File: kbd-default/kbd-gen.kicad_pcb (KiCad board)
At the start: 2 copper layers, 284.6 x 94.2 mm, 142 parts, among them CN1 BTB, CN2 BTB

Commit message: update kbd-default
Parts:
- removed the ? at (309.1, 81.9)
- removed the ? at (310.3, 81.9)
- removed the ? at (87.8, 82.5)
- added ?: , , F.Cu at (91.6, 83.0)
- added ?: , , F.Cu at (308.7, 83.0)
- added ?: , , F.Cu at (61.4, 159.2)
- added ?: , , F.Cu at (301.8, 82.8)
- added ?: , , F.Cu at (346.4, 158.4)
- added ?: , , F.Cu at (347.0, 65.0)
- added ?: , , F.Cu at (62.9, 65.2)
- moved ? 0.62 mm to (170.5, 68.1)
- moved ? 0.46 mm to (86.5, 83.0)
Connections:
- CN1 pad 33: (no net) -> VCC
- CN1 pad 34: (no net) -> GND
- CN2 pad 33: (no net) -> VCC
- CN2 pad 34: (no net) -> GND
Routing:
- net VCC: track 1589.7 -> 1602.3 mm, vias 16 -> 17
- net r4: track 391.7 -> 383.9 mm, vias 4 -> 2
- net c1: track 163.5 -> 167.5 mm
- net c3: track 139.0 -> 141.8 mm
- net r2: track 322.5 -> 319.8 mm
- net led2_17: track 148.7 -> 150.9 mm, vias 5 -> 6
- net r5: track 491.5 -> 489.6 mm
- net GND: track 1577.0 -> 1578.8 mm, vias 15 -> 14
- net S312_314: track 41.2 -> 42.9 mm
- net r3: track 408.2 -> 409.9 mm
- net S48_58: track 28.8 -> 27.3 mm
- net c4: track 83.3 -> 84.7 mm
- net r1: track 286.8 -> 288.2 mm
- net S37_38: track 29.5 -> 30.7 mm
- net S113_114: track 41.0 -> 39.9 mm
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
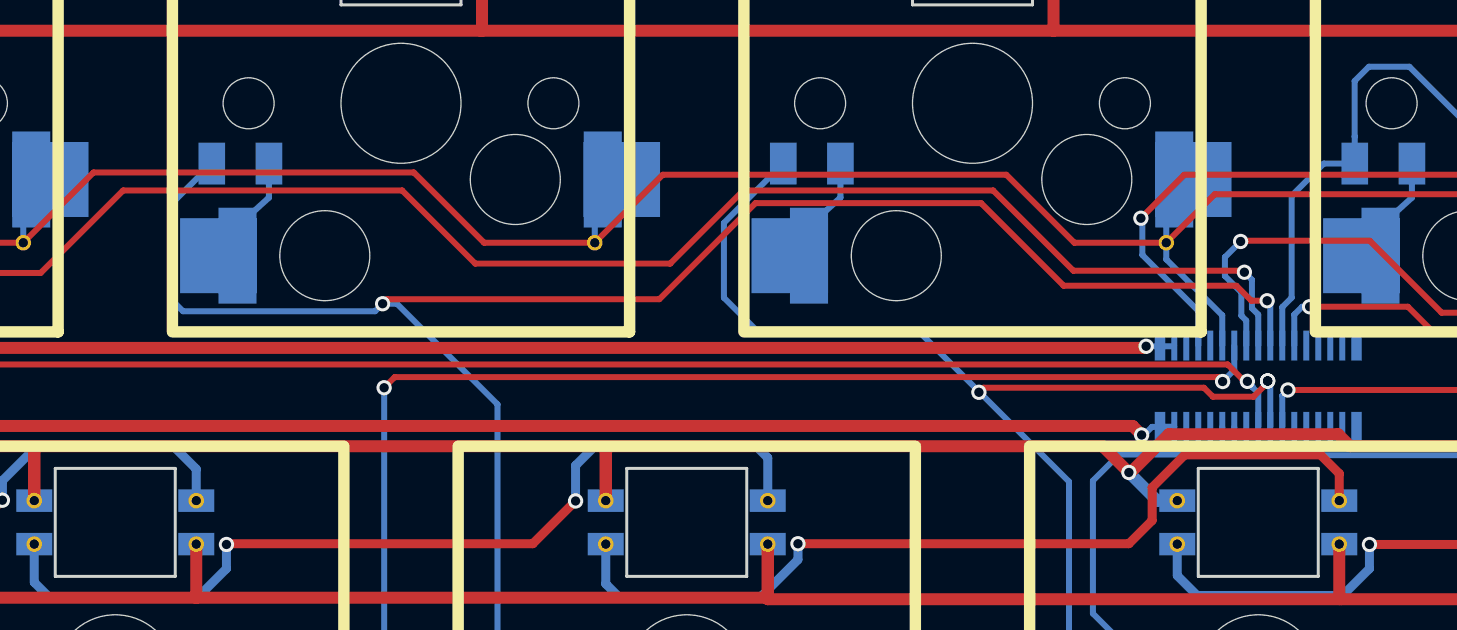
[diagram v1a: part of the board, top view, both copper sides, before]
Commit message: update default(boa) v0.2
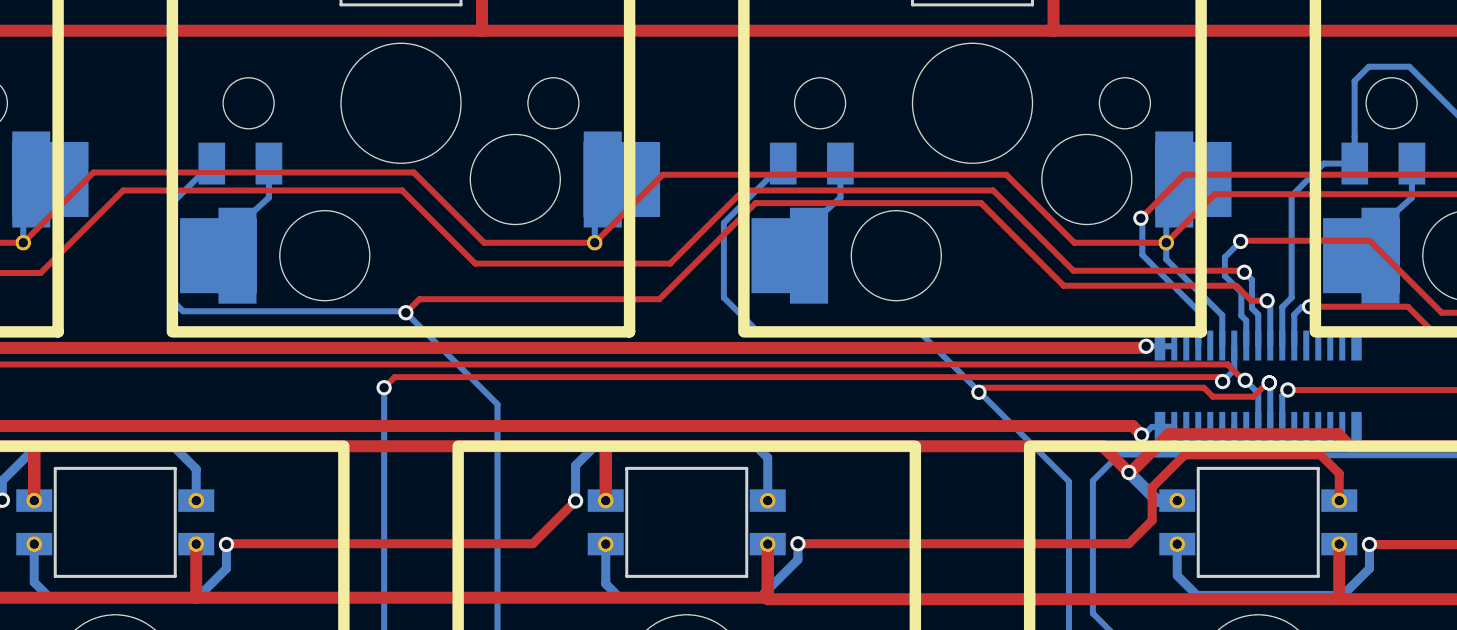
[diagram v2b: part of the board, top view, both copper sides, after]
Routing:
- net c3: track 141.8 -> 140.9 mm
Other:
- board text added: "SplitSq60(boa-hs-v0.2) by ngzh (evolved from GH60 by komar007 & jdcarpe)"
- board text removed: "split60(hs-default-v0.1) by ngzh (evolved from GH60 by komar007 & jdcarpe)"

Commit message: update
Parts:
- added ?: , , F.Cu at (79.0, 82.8)
- added ?: , , F.Cu at (312.2, 82.7)
- moved ? 0.47 mm to (189.7, 122.3)
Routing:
- net GND: track 1578.8 -> 1712.7 mm, vias 14 -> 76
- net VCC: track 1602.3 -> 1707.8 mm
- net S27_37: track 30.5 -> 25.4 mm
- net S17_16: track 52.7 -> 55.1 mm
- net c7: track 255.4 -> 254.4 mm
- net r5: track 489.6 -> 489.0 mm
- net S45_46: track 30.6 -> 30.1 mm
- net S38_39: track 31.0 -> 30.4 mm
- net S310_311: track 30.8 -> 30.2 mm
- net S311_312: track 31.1 -> 30.6 mm
- net S312_314: track 42.9 -> 42.4 mm, vias 3 -> 2
- net S512_513: track 35.1 -> 34.8 mm, vias 3 -> 2
- net S58_59: track 42.7 -> 42.4 mm, vias 3 -> 2
- net c4: vias 3 -> 2

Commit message: update anysplit60-dnav
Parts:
- removed the ? at (61.4, 159.2)
- removed the ? at (346.4, 158.4)
- removed the ? at (347.0, 65.0)
- removed the ? at (62.9, 65.2)
- added ?: MountingHole_2.5mm, Mounting_Holes:MountingHole_2.5mm, F.Cu at (344.4, 144.7)
- added ?: MountingHole_2.5mm, Mounting_Holes:MountingHole_2.5mm, F.Cu at (65.2, 144.7)
- added ?: MountingHole_2.5mm, Mounting_Holes:MountingHole_2.5mm, F.Cu at (344.4, 87.5)
- added ?: MountingHole_2.5mm, Mounting_Holes:MountingHole_2.5mm, F.Cu at (65.2, 87.5)
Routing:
- net (no net): track 0.00 -> 45.3 mm
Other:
- board text added: "anise60b(hs-v0.3) by ngzh (evolved from GH60 by komar007 & jdcarpe)"
- board text removed: "SplitSq60(boa-hs-v0.2) by ngzh (evolved from GH60 by komar007 & jdcarpe)"
